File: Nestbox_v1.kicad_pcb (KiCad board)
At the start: 2 copper layers, 100 x 91 mm, 92 parts, among them P1 RX/TX, P2 TST/RST, P3 VDD/GND, P4 NFC_PWR_SEL, Q1 SFH 3605, Q2 SFH 3605, SW1 SMD-BUTTON_2P-3.0X2.5X1.2+0.4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, U1 MSP430FR5969, U2 CR95HF, U3 TPS630250RNC, U4 RN2483, Y1 Crystal, Y2 ABM11-142-27.120MHz

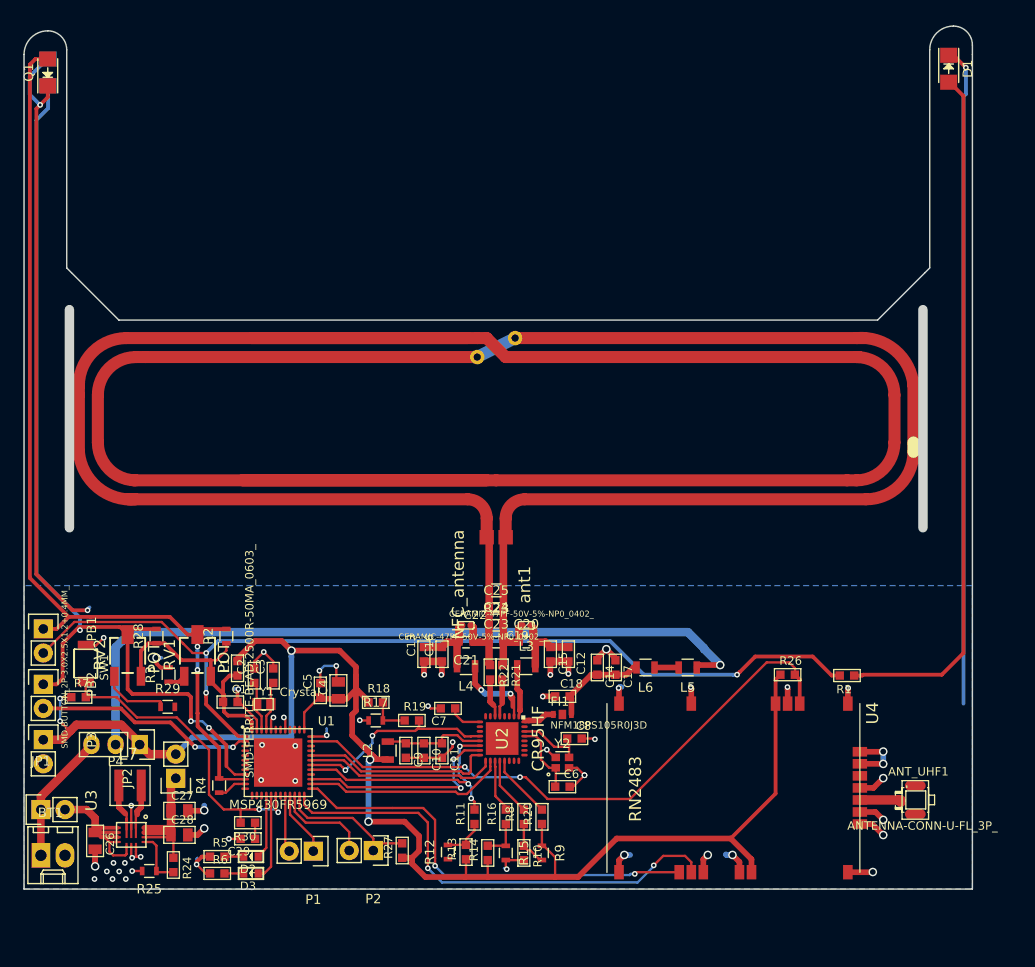
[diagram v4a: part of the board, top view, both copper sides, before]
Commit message: silk screen, stitching, top gnd plate
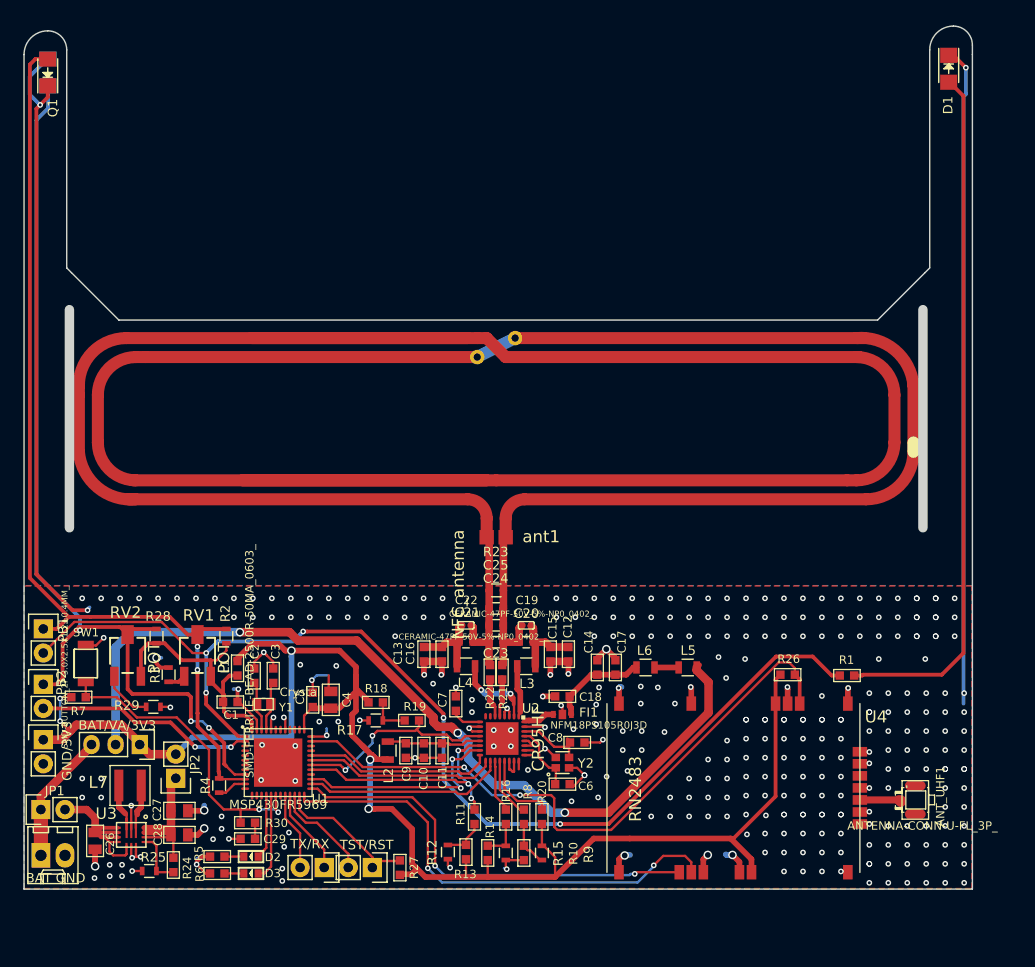
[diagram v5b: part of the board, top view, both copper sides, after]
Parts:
- BAT GND: renamed from BT1
- GND/3V3 : renamed from P3
- moved TX/RX 2.08 mm to (128.5, 140.4)
- moved R27 1.82 mm to (136.5, 140.4)
- moved TST/RST 1.80 mm to (133.6, 140.4)
- moved R29 1.51 mm to (110.5, 123.4)
- moved C5 1.28 mm to (127.3, 122.7)
- moved C4 1.28 mm to (129.2, 122.7)
- moved C7 0.97 mm to (142.4, 123.1), turned to 180 degrees
- moved C8 0.51 mm to (155.2, 127.2)
- moved C6 0.27 mm to (153.6, 131.6)
- renumbered P4 to BAT/VA/3V3, P2 to TST/RST, P1 to TX/RX
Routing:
- net /light_barrier_out: track 101.5 -> 119.5 mm, vias 3 -> 5
- net VDDA: track 78.7 -> 92.6 mm, vias 1 -> 3
- net LORA_RST_N: track 63.7 -> 68.2 mm
- net GND: track 244.0 -> 246.3 mm, vias 59 -> 346
- net Net-(P1-Pad1): track 6.88 -> 9.08 mm
- net Net-(P1-Pad2): track 6.03 -> 8.24 mm
- net Net-(R29-Pad1): track 7.62 -> 5.63 mm
- net +3V3: track 171.1 -> 169.2 mm
- net Net-(R20-Pad1): track 6.78 -> 8.18 mm
- net Net-(C10-Pad1): track 10.8 -> 10.0 mm
- net Net-(C7-Pad1): track 3.55 -> 2.94 mm
- added copper zone on F.Cu, net GND

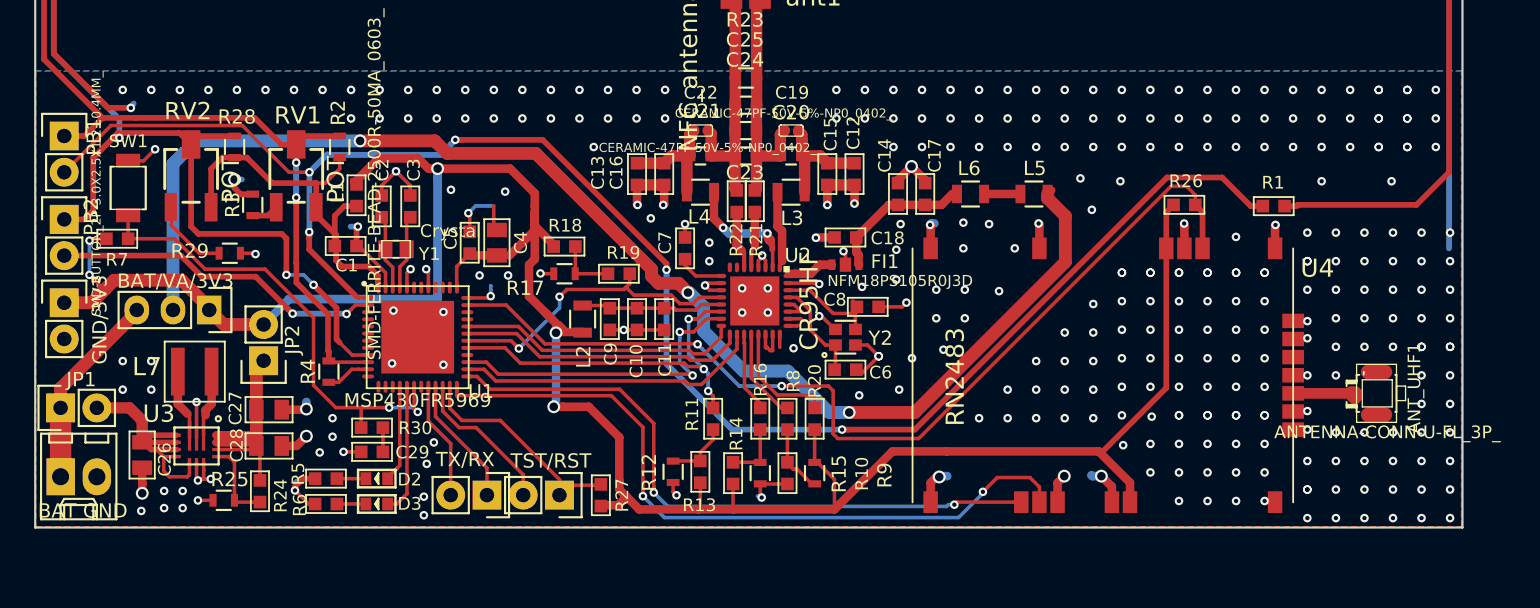
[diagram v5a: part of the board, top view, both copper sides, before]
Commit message: corrected gnd vias, added logo footprints
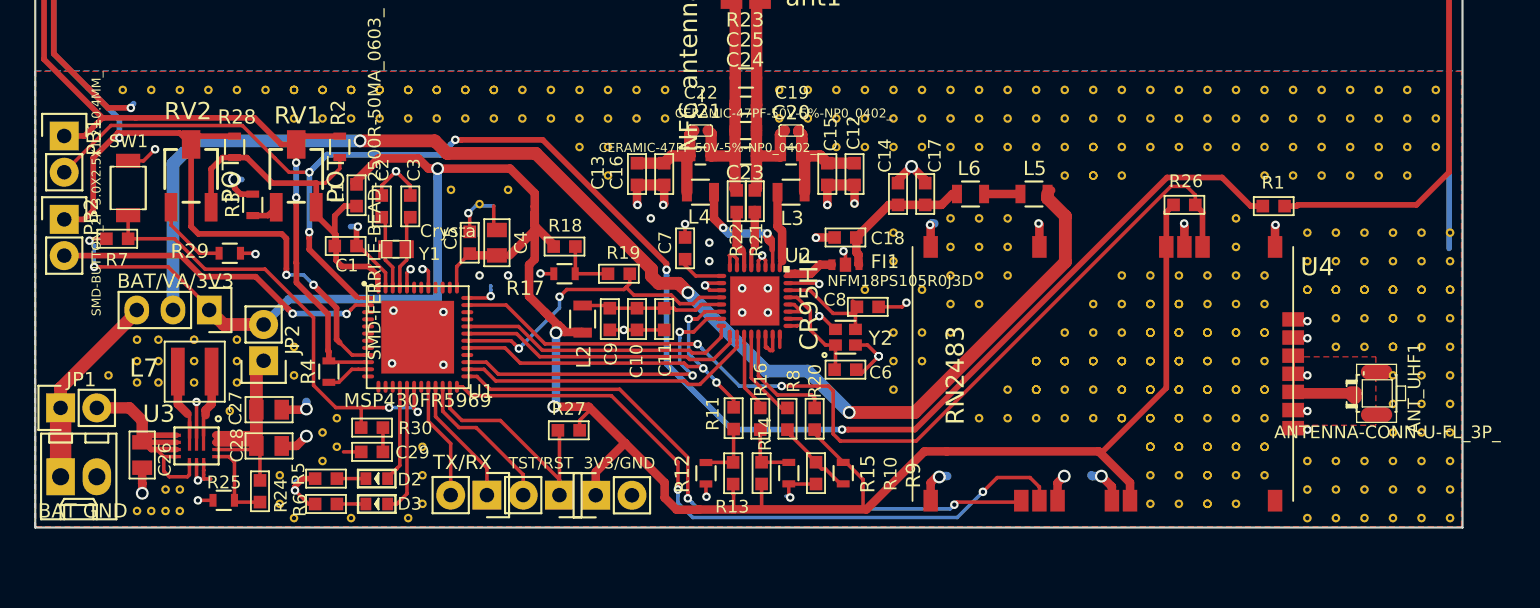
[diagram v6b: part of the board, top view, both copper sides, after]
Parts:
- added REF**: stitching_via, Octanis3:stitching_via, F.Cu at (102.0, 132.0)
- added REF**: stitching_via, Octanis3:stitching_via, F.Cu at (105.5, 132.5)
- added REF**: stitching_via, Octanis3:stitching_via, F.Cu at (163.0, 127.0)
- added REF**: stitching_via, Octanis3:stitching_via, F.Cu at (161.0, 129.0)
- added REF**: stitching_via, Octanis3:stitching_via, F.Cu at (159.0, 131.0)
- added REF**: stitching_via, Octanis3:stitching_via, F.Cu at (157.0, 133.0)
- added REF**: stitching_via, Octanis3:stitching_via, F.Cu at (181.0, 121.0)
- added REF**: stitching_via, Octanis3:stitching_via, F.Cu at (181.0, 123.0)
- added REF**: stitching_via, Octanis3:stitching_via, F.Cu at (173.0, 125.0)
- added REF** (x3): stitching_via, Octanis3:stitching_via, F.Cu at (167.0, 131.0)
- added REF** (x4): stitching_via, Octanis3:stitching_via, F.Cu at (167.0, 133.0)
- added REF**: stitching_via, Octanis3:stitching_via, F.Cu at (105.5, 131.0)
- added REF**: stitching_via, Octanis3:stitching_via, F.Cu at (165.0, 133.0)
- added REF**: stitching_via, Octanis3:stitching_via, F.Cu at (165.0, 135.0)
- added REF**: stitching_via, Octanis3:stitching_via, F.Cu at (167.0, 135.0)
- added REF**: stitching_via, Octanis3:stitching_via, F.Cu at (177.0, 139.0)
- added REF**: stitching_via, Octanis3:stitching_via, F.Cu at (175.0, 141.0)
- added REF**: stitching_via, Octanis3:stitching_via, F.Cu at (175.0, 139.0)
- added REF**: stitching_via, Octanis3:stitching_via, F.Cu at (104.0, 131.0)
- added REF**: stitching_via, Octanis3:stitching_via, F.Cu at (177.0, 141.0)
- added REF** (x3): stitching_via, Octanis3:stitching_via, F.Cu at (175.0, 137.0)
- added REF** (x3): stitching_via, Octanis3:stitching_via, F.Cu at (177.0, 133.0)
- added REF** (x3): stitching_via, Octanis3:stitching_via, F.Cu at (175.0, 133.0)
- added REF** (x2): stitching_via, Octanis3:stitching_via, F.Cu at (175.0, 135.0)
- added REF** (x2): stitching_via, Octanis3:stitching_via, F.Cu at (181.0, 137.0)
- added REF**: stitching_via, Octanis3:stitching_via, F.Cu at (183.0, 135.0)
- added REF**: stitching_via, Octanis3:stitching_via, F.Cu at (105.5, 129.5)
- added REF**: stitching_via, Octanis3:stitching_via, F.Cu at (181.0, 135.0)
- added REF** (x3): stitching_via, Octanis3:stitching_via, F.Cu at (179.0, 137.0)
- added REF** (x3): stitching_via, Octanis3:stitching_via, F.Cu at (177.0, 137.0)
- added REF**: stitching_via, Octanis3:stitching_via, F.Cu at (179.0, 135.0)
- added REF** (x2): stitching_via, Octanis3:stitching_via, F.Cu at (177.0, 135.0)
- added REF** (x2): stitching_via, Octanis3:stitching_via, F.Cu at (179.0, 141.0)
- added REF**: stitching_via, Octanis3:stitching_via, F.Cu at (104.0, 129.5)
- added REF** (x2): stitching_via, Octanis3:stitching_via, F.Cu at (179.0, 139.0)
- added REF**: stitching_via, Octanis3:stitching_via, F.Cu at (181.0, 141.0)
- added REF**: stitching_via, Octanis3:stitching_via, F.Cu at (181.0, 139.0)
- added REF** (x2): stitching_via, Octanis3:stitching_via, F.Cu at (183.0, 137.0)
- added REF**: stitching_via, Octanis3:stitching_via, F.Cu at (183.0, 139.0)
- added REF** (x2): stitching_via, Octanis3:stitching_via, F.Cu at (181.0, 133.0)
- added REF** (x2): stitching_via, Octanis3:stitching_via, F.Cu at (183.0, 133.0)
- added REF**: stitching_via, Octanis3:stitching_via, F.Cu at (104.0, 141.5)
- added REF** (x3): stitching_via, Octanis3:stitching_via, F.Cu at (179.0, 133.0)
- added REF**: stitching_via, Octanis3:stitching_via, F.Cu at (171.0, 133.0)
- added REF**: stitching_via, Octanis3:stitching_via, F.Cu at (169.0, 135.0)
- added REF**: stitching_via, Octanis3:stitching_via, F.Cu at (169.0, 133.0)
- added REF**: stitching_via, Octanis3:stitching_via, F.Cu at (171.0, 135.0)
- added REF** (x3): stitching_via, Octanis3:stitching_via, F.Cu at (169.0, 131.0)
- added REF**: stitching_via, Octanis3:stitching_via, F.Cu at (171.0, 127.0)
- added REF**: stitching_via, Octanis3:stitching_via, F.Cu at (163.0, 135.0)
- added REF**: stitching_via, Octanis3:stitching_via, F.Cu at (169.0, 129.0)
- added REF**: stitching_via, Octanis3:stitching_via, F.Cu at (105.0, 141.5)
- added REF** (x3): stitching_via, Octanis3:stitching_via, F.Cu at (175.0, 131.0)
- added REF** (x4): stitching_via, Octanis3:stitching_via, F.Cu at (177.0, 129.0)
- added REF** (x4): stitching_via, Octanis3:stitching_via, F.Cu at (175.0, 129.0)
- added REF** (x3): stitching_via, Octanis3:stitching_via, F.Cu at (173.0, 131.0)
- added REF** (x3): stitching_via, Octanis3:stitching_via, F.Cu at (171.0, 131.0)
- added REF**: stitching_via, Octanis3:stitching_via, F.Cu at (173.0, 129.0)
- added REF**: stitching_via, Octanis3:stitching_via, F.Cu at (106.0, 141.5)
- added REF**: stitching_via, Octanis3:stitching_via, F.Cu at (171.0, 129.0)
- added REF** (x2): stitching_via, Octanis3:stitching_via, F.Cu at (173.0, 135.0)
- added REF** (x2): stitching_via, Octanis3:stitching_via, F.Cu at (173.0, 133.0)
- added REF**: stitching_via, Octanis3:stitching_via, F.Cu at (106.0, 140.0)
- added REF** (x3): stitching_via, Octanis3:stitching_via, F.Cu at (177.0, 131.0)
- added REF** (x2): stitching_via, Octanis3:stitching_via, F.Cu at (175.0, 127.0)
- added REF** (x2): stitching_via, Octanis3:stitching_via, F.Cu at (177.0, 127.0)
- added REF**: stitching_via, Octanis3:stitching_via, F.Cu at (173.0, 127.0)
- added REF**: stitching_via, Octanis3:stitching_via, F.Cu at (107.0, 140.0)
- added REF**: stitching_via, Octanis3:stitching_via, F.Cu at (177.0, 125.0)
- added REF**: stitching_via, Octanis3:stitching_via, F.Cu at (175.0, 125.0)
- added REF** (x2): stitching_via, Octanis3:stitching_via, F.Cu at (181.0, 129.0)
- added REF**: stitching_via, Octanis3:stitching_via, F.Cu at (183.0, 127.0)
- added REF**: stitching_via, Octanis3:stitching_via, F.Cu at (181.0, 127.0)
- added REF**: stitching_via, Octanis3:stitching_via, F.Cu at (110.5, 134.5)
- added REF**: stitching_via, Octanis3:stitching_via, F.Cu at (107.0, 141.5)
- added REF** (x3): stitching_via, Octanis3:stitching_via, F.Cu at (179.0, 129.0)
- added REF**: stitching_via, Octanis3:stitching_via, F.Cu at (179.0, 127.0)
- added REF** (x2): stitching_via, Octanis3:stitching_via, F.Cu at (179.0, 131.0)
- added REF**: stitching_via, Octanis3:stitching_via, F.Cu at (123.0, 142.0)
- added REF**: stitching_via, Octanis3:stitching_via, F.Cu at (181.0, 131.0)
- added REF** (x2): stitching_via, Octanis3:stitching_via, F.Cu at (183.0, 129.0)
- added REF**: stitching_via, Octanis3:stitching_via, F.Cu at (183.0, 131.0)
- added REF**: stitching_via, Octanis3:stitching_via, F.Cu at (181.0, 125.0)
- added REF**: stitching_via, Octanis3:stitching_via, F.Cu at (183.0, 125.0)
- added REF**: stitching_via, Octanis3:stitching_via, F.Cu at (119.0, 142.0)
- added REF**: stitching_via, Octanis3:stitching_via, F.Cu at (179.0, 125.0)
- added REF**: stitching_via, Octanis3:stitching_via, F.Cu at (190.0, 128.0)
- added REF** (x2): stitching_via, Octanis3:stitching_via, F.Cu at (192.0, 130.0)
- added REF** (x2): stitching_via, Octanis3:stitching_via, F.Cu at (192.0, 128.0)
- added REF**: stitching_via, Octanis3:stitching_via, F.Cu at (190.0, 130.0)
- added REF** (x3): stitching_via, Octanis3:stitching_via, F.Cu at (188.0, 126.0)
- added REF** (x3): stitching_via, Octanis3:stitching_via, F.Cu at (192.0, 126.0)
- added REF**: stitching_via, Octanis3:stitching_via, F.Cu at (188.0, 130.0)
- added REF**: stitching_via, Octanis3:stitching_via, F.Cu at (188.0, 128.0)
- added REF** (x3): stitching_via, Octanis3:stitching_via, F.Cu at (190.0, 126.0)
- added REF**: stitching_via, Octanis3:stitching_via, F.Cu at (115.0, 142.0)
- added REF**: stitching_via, Octanis3:stitching_via, F.Cu at (188.0, 140.0)
- added REF**: stitching_via, Octanis3:stitching_via, F.Cu at (190.0, 142.0)
- added REF**: stitching_via, Octanis3:stitching_via, F.Cu at (190.0, 140.0)
- added REF**: stitching_via, Octanis3:stitching_via, F.Cu at (188.0, 142.0)
- added REF**: stitching_via, Octanis3:stitching_via, F.Cu at (186.0, 138.0)
- added REF**: stitching_via, Octanis3:stitching_via, F.Cu at (190.0, 138.0)
- added REF**: stitching_via, Octanis3:stitching_via, F.Cu at (186.0, 142.0)
- added REF**: stitching_via, Octanis3:stitching_via, F.Cu at (186.0, 140.0)
- added REF**: stitching_via, Octanis3:stitching_via, F.Cu at (188.0, 138.0)
- added REF** (x2): stitching_via, Octanis3:stitching_via, F.Cu at (186.0, 126.0)
- added REF**: stitching_via, Octanis3:stitching_via, F.Cu at (114.0, 141.0)
- added REF**: stitching_via, Octanis3:stitching_via, F.Cu at (188.0, 124.0)
- added REF**: stitching_via, Octanis3:stitching_via, F.Cu at (190.0, 124.0)
- added REF**: stitching_via, Octanis3:stitching_via, F.Cu at (186.0, 122.0)
- added REF**: stitching_via, Octanis3:stitching_via, F.Cu at (190.0, 122.0)
- added REF**: stitching_via, Octanis3:stitching_via, F.Cu at (188.0, 122.0)
- added REF**: stitching_via, Octanis3:stitching_via, F.Cu at (114.0, 139.0)
- added REF**: stitching_via, Octanis3:stitching_via, F.Cu at (186.0, 124.0)
- added REF**: stitching_via, Octanis3:stitching_via, F.Cu at (194.0, 136.0)
- added REF**: stitching_via, Octanis3:stitching_via, F.Cu at (196.0, 136.0)
- added REF**: stitching_via, Octanis3:stitching_via, F.Cu at (192.0, 136.0)
- added REF**: stitching_via, Octanis3:stitching_via, F.Cu at (192.0, 134.0)
- added REF**: stitching_via, Octanis3:stitching_via, F.Cu at (194.0, 132.0)
- added REF**: stitching_via, Octanis3:stitching_via, F.Cu at (194.0, 134.0)
- added REF**: stitching_via, Octanis3:stitching_via, F.Cu at (196.0, 134.0)
- added REF**: stitching_via, Octanis3:stitching_via, F.Cu at (192.0, 132.0)
- added REF**: stitching_via, Octanis3:stitching_via, F.Cu at (196.0, 132.0)
- added REF**: stitching_via, Octanis3:stitching_via, F.Cu at (115.0, 130.0)
- added REF**: stitching_via, Octanis3:stitching_via, F.Cu at (194.0, 142.0)
- added REF**: stitching_via, Octanis3:stitching_via, F.Cu at (196.0, 142.0)
- added REF**: stitching_via, Octanis3:stitching_via, F.Cu at (192.0, 142.0)
- added REF**: stitching_via, Octanis3:stitching_via, F.Cu at (192.0, 140.0)
- added REF**: stitching_via, Octanis3:stitching_via, F.Cu at (194.0, 138.0)
- added REF**: stitching_via, Octanis3:stitching_via, F.Cu at (194.0, 140.0)
- added REF**: stitching_via, Octanis3:stitching_via, F.Cu at (196.0, 140.0)
- added REF**: stitching_via, Octanis3:stitching_via, F.Cu at (192.0, 138.0)
- added REF**: stitching_via, Octanis3:stitching_via, F.Cu at (196.0, 138.0)
- added REF**: stitching_via, Octanis3:stitching_via, F.Cu at (194.0, 130.0)
- added REF**: stitching_via, Octanis3:stitching_via, F.Cu at (115.0, 132.0)
- added REF**: stitching_via, Octanis3:stitching_via, F.Cu at (196.0, 130.0)
- added REF** (x2): stitching_via, Octanis3:stitching_via, F.Cu at (194.0, 126.0)
- added REF**: stitching_via, Octanis3:stitching_via, F.Cu at (194.0, 128.0)
- added REF**: stitching_via, Octanis3:stitching_via, F.Cu at (196.0, 128.0)
- added REF** (x2): stitching_via, Octanis3:stitching_via, F.Cu at (196.0, 126.0)
- added REF**: stitching_via, Octanis3:stitching_via, F.Cu at (118.0, 137.0)
- added REF**: stitching_via, Octanis3:stitching_via, F.Cu at (192.0, 124.0)
- added REF**: stitching_via, Octanis3:stitching_via, F.Cu at (194.0, 122.0)
- added REF**: stitching_via, Octanis3:stitching_via, F.Cu at (194.0, 124.0)
- added REF**: stitching_via, Octanis3:stitching_via, F.Cu at (196.0, 124.0)
- added REF**: stitching_via, Octanis3:stitching_via, F.Cu at (192.0, 122.0)
- added REF**: stitching_via, Octanis3:stitching_via, F.Cu at (196.0, 122.0)
- added REF**: stitching_via, Octanis3:stitching_via, F.Cu at (183.0, 118.0)
- added REF**: stitching_via, Octanis3:stitching_via, F.Cu at (185.0, 118.0)
- added REF**: stitching_via, Octanis3:stitching_via, F.Cu at (175.0, 116.0)
- added REF**: stitching_via, Octanis3:stitching_via, F.Cu at (118.0, 135.0)
- added REF**: stitching_via, Octanis3:stitching_via, F.Cu at (173.0, 116.0)
- added REF**: stitching_via, Octanis3:stitching_via, F.Cu at (173.0, 118.0)
- added REF** (x2): stitching_via, Octanis3:stitching_via, F.Cu at (171.0, 118.0)
- added REF** (x2): stitching_via, Octanis3:stitching_via, F.Cu at (171.0, 116.0)
- added REF**: stitching_via, Octanis3:stitching_via, F.Cu at (169.0, 118.0)
- added REF**: stitching_via, Octanis3:stitching_via, F.Cu at (169.0, 116.0)
- added REF**: stitching_via, Octanis3:stitching_via, F.Cu at (155.0, 116.0)
- added REF**: stitching_via, Octanis3:stitching_via, F.Cu at (153.0, 116.0)
- added REF**: stitching_via, Octanis3:stitching_via, F.Cu at (111.0, 132.5)
- added REF**: stitching_via, Octanis3:stitching_via, F.Cu at (117.0, 136.0)
- added REF**: stitching_via, Octanis3:stitching_via, F.Cu at (149.0, 114.0)
- added REF**: stitching_via, Octanis3:stitching_via, F.Cu at (153.0, 114.0)
- added REF**: stitching_via, Octanis3:stitching_via, F.Cu at (151.0, 114.0)
- added REF**: stitching_via, Octanis3:stitching_via, F.Cu at (149.0, 112.0)
- added REF**: stitching_via, Octanis3:stitching_via, F.Cu at (153.0, 112.0)
- added REF**: stitching_via, Octanis3:stitching_via, F.Cu at (151.0, 112.0)
- added REF**: stitching_via, Octanis3:stitching_via, F.Cu at (161.0, 116.0)
- added REF**: stitching_via, Octanis3:stitching_via, F.Cu at (161.0, 114.0)
- added REF**: stitching_via, Octanis3:stitching_via, F.Cu at (163.0, 116.0)
- added REF**: stitching_via, Octanis3:stitching_via, F.Cu at (157.0, 114.0)
- added REF**: stitching_via, Octanis3:stitching_via, F.Cu at (117.0, 138.0)
- added REF**: stitching_via, Octanis3:stitching_via, F.Cu at (155.0, 114.0)
- added REF**: stitching_via, Octanis3:stitching_via, F.Cu at (159.0, 114.0)
- added REF**: stitching_via, Octanis3:stitching_via, F.Cu at (159.0, 116.0)
- added REF**: stitching_via, Octanis3:stitching_via, F.Cu at (157.0, 116.0)
- added REF**: stitching_via, Octanis3:stitching_via, F.Cu at (157.0, 112.0)
- added REF**: stitching_via, Octanis3:stitching_via, F.Cu at (161.0, 112.0)
- added REF**: stitching_via, Octanis3:stitching_via, F.Cu at (159.0, 112.0)
- added REF**: stitching_via, Octanis3:stitching_via, F.Cu at (155.0, 112.0)
- added REF**: stitching_via, Octanis3:stitching_via, F.Cu at (163.0, 112.0)
- added REF**: stitching_via, Octanis3:stitching_via, F.Cu at (163.0, 114.0)
- added REF**: stitching_via, Octanis3:stitching_via, F.Cu at (124.0, 141.0)
- added REF**: stitching_via, Octanis3:stitching_via, F.Cu at (171.0, 114.0)
- added REF**: stitching_via, Octanis3:stitching_via, F.Cu at (167.0, 114.0)
- added REF**: stitching_via, Octanis3:stitching_via, F.Cu at (165.0, 114.0)
- added REF**: stitching_via, Octanis3:stitching_via, F.Cu at (165.0, 116.0)
- added REF**: stitching_via, Octanis3:stitching_via, F.Cu at (169.0, 114.0)
- added REF**: stitching_via, Octanis3:stitching_via, F.Cu at (167.0, 116.0)
- added REF**: stitching_via, Octanis3:stitching_via, F.Cu at (167.0, 112.0)
- added REF**: stitching_via, Octanis3:stitching_via, F.Cu at (171.0, 112.0)
- added REF**: stitching_via, Octanis3:stitching_via, F.Cu at (169.0, 112.0)
- added REF**: stitching_via, Octanis3:stitching_via, F.Cu at (165.0, 112.0)
- added REF**: stitching_via, Octanis3:stitching_via, F.Cu at (124.0, 139.0)
- added REF**: stitching_via, Octanis3:stitching_via, F.Cu at (173.0, 112.0)
- added REF**: stitching_via, Octanis3:stitching_via, F.Cu at (173.0, 114.0)
- added REF**: stitching_via, Octanis3:stitching_via, F.Cu at (181.0, 116.0)
- added REF**: stitching_via, Octanis3:stitching_via, F.Cu at (181.0, 114.0)
- added REF**: stitching_via, Octanis3:stitching_via, F.Cu at (183.0, 116.0)
- added REF**: stitching_via, Octanis3:stitching_via, F.Cu at (177.0, 114.0)
- added REF**: stitching_via, Octanis3:stitching_via, F.Cu at (175.0, 114.0)
- added REF**: stitching_via, Octanis3:stitching_via, F.Cu at (179.0, 114.0)
- added REF**: stitching_via, Octanis3:stitching_via, F.Cu at (179.0, 116.0)
- added REF**: stitching_via, Octanis3:stitching_via, F.Cu at (177.0, 116.0)
- added REF**: stitching_via, Octanis3:stitching_via, F.Cu at (124.0, 137.0)
- added REF**: stitching_via, Octanis3:stitching_via, F.Cu at (177.0, 112.0)
- added REF**: stitching_via, Octanis3:stitching_via, F.Cu at (181.0, 112.0)
- added REF**: stitching_via, Octanis3:stitching_via, F.Cu at (179.0, 112.0)
- added REF**: stitching_via, Octanis3:stitching_via, F.Cu at (175.0, 112.0)
- added REF**: stitching_via, Octanis3:stitching_via, F.Cu at (183.0, 112.0)
- added REF**: stitching_via, Octanis3:stitching_via, F.Cu at (183.0, 114.0)
- added REF**: stitching_via, Octanis3:stitching_via, F.Cu at (191.0, 112.0)
- added REF**: stitching_via, Octanis3:stitching_via, F.Cu at (185.0, 112.0)
- added REF**: stitching_via, Octanis3:stitching_via, F.Cu at (187.0, 112.0)
- added REF**: stitching_via, Octanis3:stitching_via, F.Cu at (189.0, 112.0)
- added REF**: stitching_via, Octanis3:stitching_via, F.Cu at (137.0, 118.0)
- added REF**: stitching_via, Octanis3:stitching_via, F.Cu at (185.0, 114.0)
- added REF**: stitching_via, Octanis3:stitching_via, F.Cu at (187.0, 114.0)
- added REF**: stitching_via, Octanis3:stitching_via, F.Cu at (185.0, 116.0)
- added REF**: stitching_via, Octanis3:stitching_via, F.Cu at (187.0, 116.0)
- added REF**: stitching_via, Octanis3:stitching_via, F.Cu at (189.0, 116.0)
- added REF**: stitching_via, Octanis3:stitching_via, F.Cu at (191.0, 116.0)
- added REF**: stitching_via, Octanis3:stitching_via, F.Cu at (189.0, 114.0)
- added REF**: stitching_via, Octanis3:stitching_via, F.Cu at (191.0, 114.0)
- added REF**: stitching_via, Octanis3:stitching_via, F.Cu at (187.0, 118.0)
- added REF**: stitching_via, Octanis3:stitching_via, F.Cu at (189.0, 118.0)
- added REF**: stitching_via, Octanis3:stitching_via, F.Cu at (135.0, 116.0)
- added REF**: stitching_via, Octanis3:stitching_via, F.Cu at (191.0, 118.0)
- added REF**: stitching_via, Octanis3:stitching_via, F.Cu at (193.0, 118.0)
- added REF**: stitching_via, Octanis3:stitching_via, F.Cu at (193.0, 116.0)
- added REF**: stitching_via, Octanis3:stitching_via, F.Cu at (195.0, 116.0)
- added REF**: stitching_via, Octanis3:stitching_via, F.Cu at (193.0, 114.0)
- added REF**: stitching_via, Octanis3:stitching_via, F.Cu at (195.0, 114.0)
- added REF**: stitching_via, Octanis3:stitching_via, F.Cu at (193.0, 112.0)
- added REF**: stitching_via, Octanis3:stitching_via, F.Cu at (195.0, 112.0)
- added REF**: stitching_via, Octanis3:stitching_via, F.Cu at (137.0, 116.0)
- added REF**: stitching_via, Octanis3:stitching_via, F.Cu at (130.0, 119.0)
- added REF**: stitching_via, Octanis3:stitching_via, F.Cu at (128.0, 120.0)
- added REF**: stitching_via, Octanis3:stitching_via, F.Cu at (111.0, 131.0)
- added REF**: stitching_via, Octanis3:stitching_via, F.Cu at (126.0, 119.0)
- added REF**: stitching_via, Octanis3:stitching_via, F.Cu at (137.0, 114.0)
- added REF**: stitching_via, Octanis3:stitching_via, F.Cu at (135.0, 114.0)
- added REF**: stitching_via, Octanis3:stitching_via, F.Cu at (141.0, 114.0)
- added REF**: stitching_via, Octanis3:stitching_via, F.Cu at (139.0, 114.0)
- added REF**: stitching_via, Octanis3:stitching_via, F.Cu at (117.0, 114.0)
- added REF**: stitching_via, Octanis3:stitching_via, F.Cu at (119.0, 114.0)
- added REF**: stitching_via, Octanis3:stitching_via, F.Cu at (133.0, 114.0)
- added REF**: stitching_via, Octanis3:stitching_via, F.Cu at (131.0, 114.0)
- added REF**: stitching_via, Octanis3:stitching_via, F.Cu at (129.0, 114.0)
- added REF**: stitching_via, Octanis3:stitching_via, F.Cu at (111.0, 129.5)
- added REF**: stitching_via, Octanis3:stitching_via, F.Cu at (127.0, 114.0)
- added REF**: stitching_via, Octanis3:stitching_via, F.Cu at (123.0, 114.0)
- added REF**: stitching_via, Octanis3:stitching_via, F.Cu at (121.0, 114.0)
- added REF**: stitching_via, Octanis3:stitching_via, F.Cu at (125.0, 114.0)
- added REF**: stitching_via, Octanis3:stitching_via, F.Cu at (115.0, 114.0)
- added REF** (x2): stitching_via, Octanis3:stitching_via, F.Cu at (125.0, 112.0)
- added REF** (x2): stitching_via, Octanis3:stitching_via, F.Cu at (123.0, 112.0)
- added REF** (x2): stitching_via, Octanis3:stitching_via, F.Cu at (129.0, 112.0)
- added REF** (x2): stitching_via, Octanis3:stitching_via, F.Cu at (127.0, 112.0)
- added REF**: stitching_via, Octanis3:stitching_via, F.Cu at (105.0, 112.0)
- added REF**: stitching_via, Octanis3:stitching_via, F.Cu at (108.0, 129.5)
- added REF**: stitching_via, Octanis3:stitching_via, F.Cu at (107.0, 112.0)
- added REF** (x2): stitching_via, Octanis3:stitching_via, F.Cu at (121.0, 112.0)
- added REF** (x2): stitching_via, Octanis3:stitching_via, F.Cu at (119.0, 112.0)
- added REF** (x2): stitching_via, Octanis3:stitching_via, F.Cu at (117.0, 112.0)
- added REF** (x2): stitching_via, Octanis3:stitching_via, F.Cu at (115.0, 112.0)
- added REF**: stitching_via, Octanis3:stitching_via, F.Cu at (111.0, 112.0)
- added REF**: stitching_via, Octanis3:stitching_via, F.Cu at (109.0, 112.0)
- added REF**: stitching_via, Octanis3:stitching_via, F.Cu at (113.0, 112.0)
- added REF**: stitching_via, Octanis3:stitching_via, F.Cu at (103.0, 112.0)
- added REF**: stitching_via, Octanis3:stitching_via, F.Cu at (137.0, 112.0)
- added REF**: stitching_via, Octanis3:stitching_via, F.Cu at (108.0, 131.0)
- added REF**: stitching_via, Octanis3:stitching_via, F.Cu at (135.0, 112.0)
- added REF**: stitching_via, Octanis3:stitching_via, F.Cu at (141.0, 112.0)
- added REF**: stitching_via, Octanis3:stitching_via, F.Cu at (139.0, 112.0)
- added REF**: stitching_via, Octanis3:stitching_via, F.Cu at (133.0, 112.0)
- added REF**: stitching_via, Octanis3:stitching_via, F.Cu at (131.0, 112.0)
- added REF**: stitching_via, Octanis3:stitching_via, F.Cu at (108.0, 132.5)
- added REF**: stitching_via, Octanis3:stitching_via, F.Cu at (155.0, 126.0)
- added REF**: stitching_via, Octanis3:stitching_via, F.Cu at (157.0, 124.0)
- added REF**: stitching_via, Octanis3:stitching_via, F.Cu at (157.0, 122.0)
- added REF**: stitching_via, Octanis3:stitching_via, F.Cu at (157.0, 129.0)
- added REF**: stitching_via, Octanis3:stitching_via, F.Cu at (157.0, 131.0)
- added REF**: stitching_via, Octanis3:stitching_via, F.Cu at (159.0, 129.0)
- added REF**: stitching_via, Octanis3:stitching_via, F.Cu at (159.0, 126.0)
- added REF**: stitching_via, Octanis3:stitching_via, F.Cu at (104.0, 132.5)
- added REF**: stitching_via, Octanis3:stitching_via, F.Cu at (161.0, 127.0)
- added REF**: stitching_via, Octanis3:stitching_via, F.Cu at (161.0, 121.0)
- added REF**: stitching_via, Octanis3:stitching_via, F.Cu at (161.0, 123.0)
- added REF**: stitching_via, Octanis3:stitching_via, F.Cu at (161.0, 125.0)
- added REF**: stitching_via, Octanis3:stitching_via, F.Cu at (163.0, 125.0)
- added REF**: stitching_via, Octanis3:stitching_via, F.Cu at (163.0, 123.0)
- added REF**: stitching_via, Octanis3:stitching_via, F.Cu at (163.0, 121.0)
- added REF**: stitching_via, Octanis3:stitching_via, F.Cu at (165.0, 121.0)
- added REF**: stitching_via, Octanis3:stitching_via, F.Cu at (165.0, 123.0)
- added REF**: stitching_via, Octanis3:stitching_via, F.Cu at (165.0, 125.0)
- 3V3/GND: renamed from GND/3V3 
- moved 3V3/GND 39.6 mm to (136.1, 140.4), turned to 0 degrees
- moved R27 5.08 mm to (134.2, 135.8), turned to 90 degrees
- moved R12 2.30 mm to (143.9, 138.9)
- moved R13 2.30 mm to (145.8, 138.9)
- moved R10 2.00 mm to (151.6, 138.8)
- moved R14 2.00 mm to (147.8, 138.8)
- moved R15 2.00 mm to (149.7, 138.8)
- moved R9 2.00 mm to (153.5, 138.8)
- moved R11 1.43 mm to (145.8, 135.0)
- moved U4 0.10 mm to (158.3, 123.0)
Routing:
- net Net-(P2-Pad1): track 15.5 -> 17.9 mm
- net GND: track 246.3 -> 248.3 mm, vias 346 -> 58
- net LORA_RX: track 50.4 -> 48.8 mm
- net LORA_TX: track 45.6 -> 44.5 mm
- net VDDA: track 92.6 -> 91.6 mm
- net Net-(R10-Pad2): track 4.86 -> 5.67 mm
- net NFC_IRQ_N: track 26.7 -> 27.2 mm
- net (no net): vias 0 -> 5
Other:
- rule trace_min: 0.2 -> 0.15
- rule via_min_size: 0.4 -> 0.3

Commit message: added logo
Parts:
- removed the REF** at (123.0, 142.0)
- removed the REF** at (119.0, 142.0)
- removed the REF** at (190.0, 142.0)
- removed the REF** at (188.0, 142.0)
- removed the REF** at (186.0, 142.0)
- removed the REF** at (196.0, 136.0)
- removed the REF** at (196.0, 134.0)
- removed the REF** at (196.0, 132.0)
- removed the REF** at (194.0, 142.0)
- removed the REF** at (196.0, 142.0)
- removed the REF** at (192.0, 142.0)
- removed the REF** at (196.0, 140.0)
- removed the REF** at (196.0, 138.0)
- removed the REF** at (196.0, 130.0)
- removed the REF** at (196.0, 128.0)
- removed the REF** at (196.0, 126.0) (x2)
- removed the REF** at (196.0, 124.0)
- removed the REF** at (196.0, 122.0)
- removed the REF** at (124.0, 141.0)
- removed the REF** at (124.0, 139.0)
- removed the REF** at (124.0, 137.0)
- added G***: LOGO, Octanis3:octanis3_logo, F.Cu at (115.5, 93.0)
- added G***: LOGO, Octanis3:octanis_open_incubator_logo, F.Cu at (179.0, 93.0)
- added REF**: stitching_via, Octanis3:stitching_via, F.Cu at (102.0, 126.5)
- added REF**: stitching_via, Octanis3:stitching_via, F.Cu at (100.0, 126.5)
- added REF**: stitching_via, Octanis3:stitching_via, F.Cu at (98.0, 126.5)
- added REF**: stitching_via, Octanis3:stitching_via, F.Cu at (98.0, 128.5)
- added REF**: stitching_via, Octanis3:stitching_via, F.Cu at (98.0, 130.5)
- added REF**: stitching_via, Octanis3:stitching_via, F.Cu at (127.0, 120.1)
- added REF**: stitching_via, Octanis3:stitching_via, F.Cu at (129.0, 120.1)
- added REF**: stitching_via, Octanis3:stitching_via, F.Cu at (126.0, 122.0)
- added REF**: stitching_via, Octanis3:stitching_via, F.Cu at (128.0, 125.0)
- added REF**: stitching_via, Octanis3:stitching_via, F.Cu at (130.0, 125.0)
- added REF**: stitching_via, Octanis3:stitching_via, F.Cu at (100.0, 128.5)
- moved REF** 1.00 mm to (128.0, 119.0)
- moved REF** 0.50 mm to (115.0, 141.5)
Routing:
- net +3V3: track 168.7 -> 169.6 mm
- net GND: vias 58 -> 57
- net (no net): vias 5 -> 2
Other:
- board text added: "Octanis 3: Digital Nestbox PCB v1.0 nestbox.octanis.org"

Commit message: generated gerber files
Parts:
- removed the REF** at (102.0, 126.5)
- removed the REF** at (100.0, 126.5)
- removed the REF** at (98.0, 126.5)
- removed the REF** at (98.0, 128.5)
- removed the REF** at (98.0, 130.5)
- removed the REF** at (102.0, 132.0)
- removed the REF** at (104.0, 132.5)
- removed the REF** at (104.0, 131.0)
- removed the REF** at (104.0, 129.5)
- removed the REF** at (100.0, 128.5)
- added REF**: stitching_via, Octanis3:stitching_via, F.Cu at (98.9, 127.2)
- added REF**: stitching_via, Octanis3:stitching_via, F.Cu at (97.8, 131.5)
- added REF**: stitching_via, Octanis3:stitching_via, F.Cu at (100.9, 130.4)
- added REF**: stitching_via, Octanis3:stitching_via, F.Cu at (102.6, 130.3)
- added REF**: stitching_via, Octanis3:stitching_via, F.Cu at (149.5, 130.5)
- added REF**: stitching_via, Octanis3:stitching_via, F.Cu at (151.5, 130.5)
- added REF**: stitching_via, Octanis3:stitching_via, F.Cu at (150.5, 130.0)
- moved SW1 10.2 mm to (98.9, 128.0), turned to 90 degrees
- moved R7 4.57 mm to (101.3, 126.8), turned to 0 degrees
- moved PB2 0.61 mm to (98.9, 120.5)
- moved ant1 0.09 mm to (146.7, 104.5)
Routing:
- net (no net): track 7.61 -> 0.00 mm
- net +3V3: track 169.6 -> 162.1 mm, vias 5 -> 3
- net +BATT: track 13.9 -> 17.7 mm
- net GND: track 248.3 -> 246.1 mm, vias 57 -> 56
- net Net-(R30-Pad1): track 33.0 -> 34.4 mm
